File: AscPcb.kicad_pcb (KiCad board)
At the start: 2 copper layers, 116 x 78.7 mm, 83 parts, among them J1 12402012E212A, J10 Conn_01x02_Pin, J11 Conn_01x02_Pin, J12 Conn_01x02_Pin, J13 Conn_01x12_Pin, J14 Conn_01x02_Pin, J15 Conn_01x02_Pin, J16 Conn_01x02_Pin, J2 B2B-PH-K-S(LF)(SN), J3 Conn_01x02_Pin, J3 Conn_01x10_Pin, J4 Conn_01x06_Pin, J5 Screw_Terminal_01x02, J6 Conn_01x02_Pin, J7 Conn_01x02_Pin, J8 Conn_01x03_Pin, J9 Screw_Terminal_01x02, Q1 Q_NMOS_DGS, Q4 BC817, Q5 BC817, SW1 TL3305AF260QG, SW2 TL3305AF260QG, U1 ESP32-C3-WROOM-02-N4, U2 BQ24040DSQR, U3 TLV75801PDRVR, U4 CP2102N-A02-GQFN24R, U5 LTC3625EDE_PBF, U6 BMI270, U8 AP62300TWU

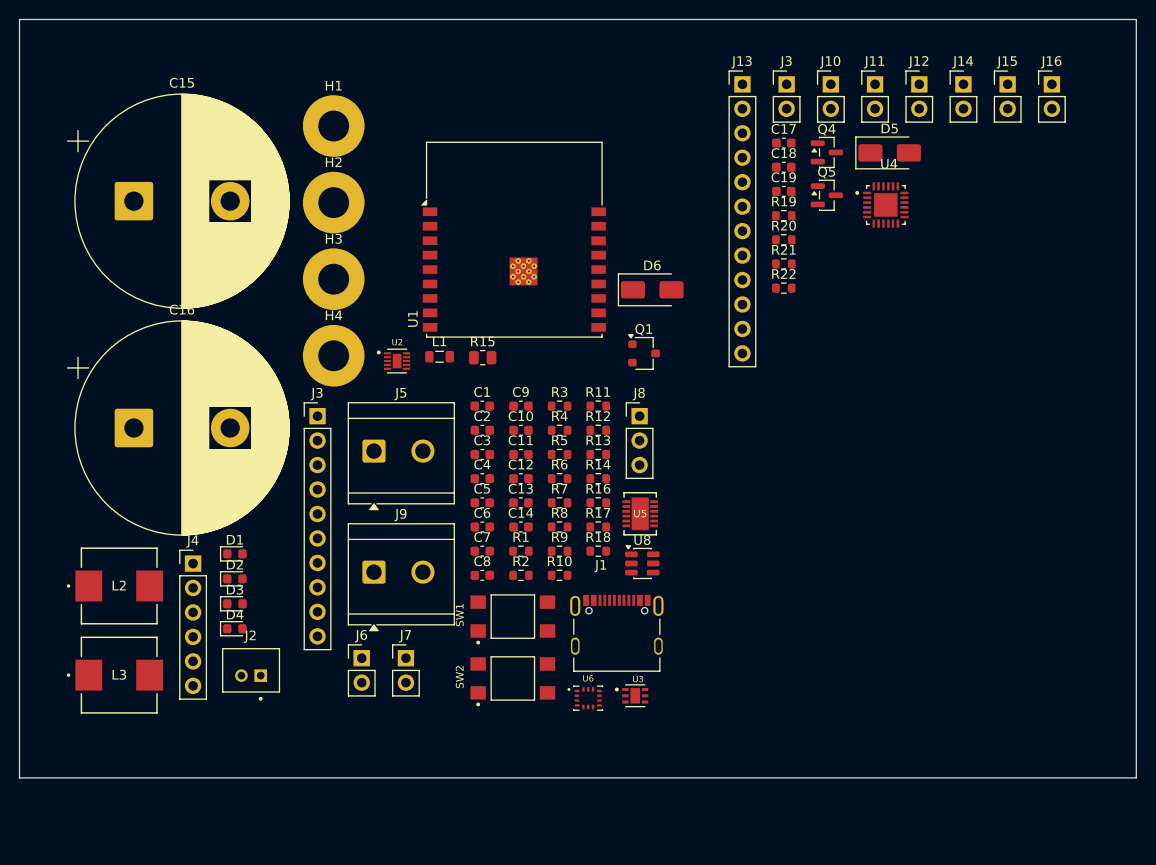
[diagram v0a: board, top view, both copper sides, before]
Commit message: add schmitt trigger
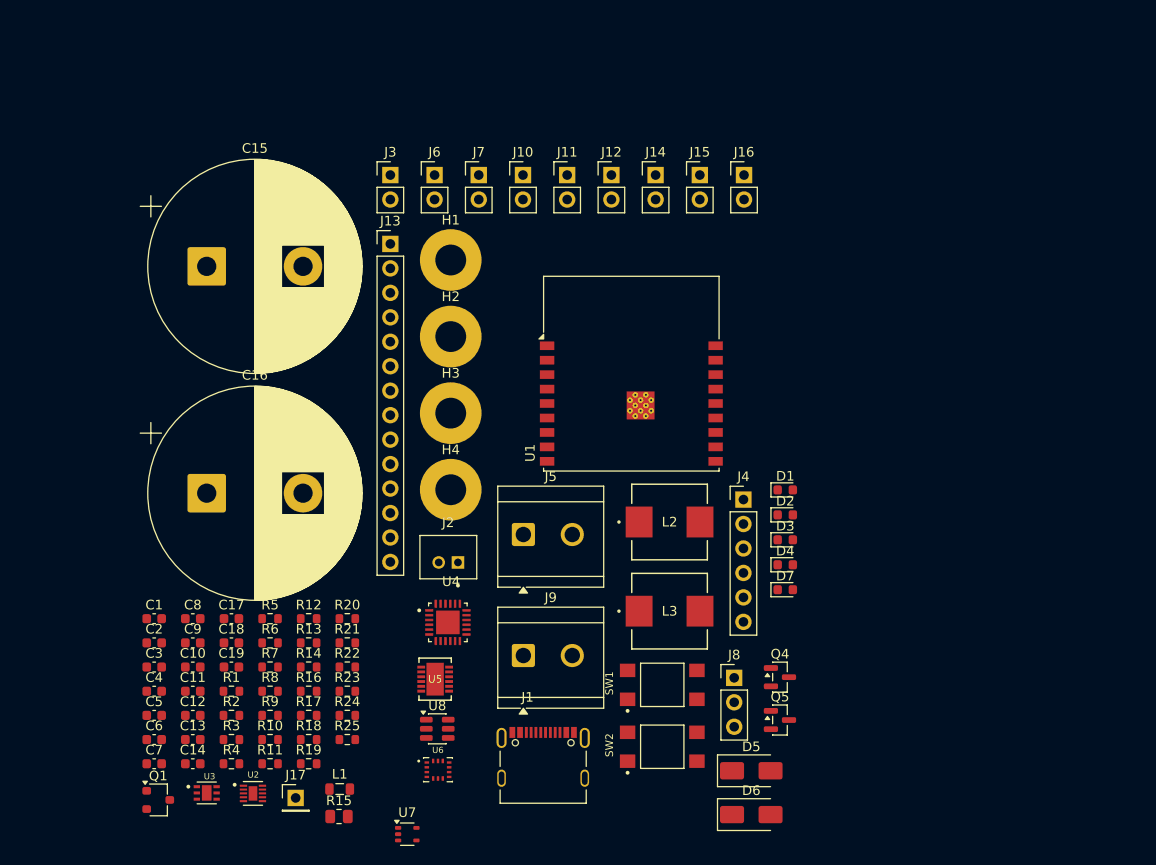
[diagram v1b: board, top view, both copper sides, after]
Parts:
- removed the J3 at (127.3, 84.1)
- removed the J3 at (176.0, 49.7)
- added D7: GREEN, LED_SMD:LED_0603_1608Metric, F.Cu at (175.9, 102.1)
- added J17: Conn_01x01_Pin, Connector_PinHeader_2.54mm:PinHeader_1x01_P2.54mm_Vertical, F.Cu at (125.1, 123.7)
- added J3: Conn_01x02_Pin, Connector_PinHeader_2.54mm:PinHeader_1x02_P2.54mm_Vertical, F.Cu at (134.9, 59.1)
- added R23: 10k, Resistor_SMD:R_0603_1608Metric, F.Cu at (130.4, 112.7)
- added R24: 10k, Resistor_SMD:R_0603_1608Metric, F.Cu at (130.4, 115.2)
- added R25: 150, Resistor_SMD:R_0603_1608Metric, F.Cu at (130.4, 117.7)
- added U7: 74LVC1G07, Package_TO_SOT_SMD:SOT-353_SC-70-5, F.Cu at (136.7, 127.5)
- J13: value Conn_01x12_Pin -> Conn_01x14_Pin; footprint Connector_PinHeader_2.54mm:PinHeader_1x12_P2.54mm_Vertical -> Connector_PinHeader_2.54mm:PinHeader_1x14_P2.54mm_Vertical
- moved C17 75.7 mm to (118.4, 105.1)
- moved C18 75.7 mm to (118.4, 107.6)
- moved C19 75.7 mm to (118.4, 110.2)
- moved R19 75.3 mm to (126.4, 120.2)
- moved Q1 68.5 mm to (110.8, 124.0)
- moved D5 65.7 mm to (172.4, 120.9)
- moved U4 62.8 mm to (140.9, 105.5)
- moved R22 60.0 mm to (130.4, 110.2)
- moved R20 60.0 mm to (130.4, 105.1)
- moved R21 60.0 mm to (130.4, 107.6)
- moved J4 57.5 mm to (171.6, 92.8)
- moved L2 57.5 mm to (163.9, 95.1)
- moved L3 57.5 mm to (163.9, 104.4)
- moved D1 57.5 mm to (175.9, 91.8)
- moved D2 57.5 mm to (175.9, 94.4)
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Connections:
- J13 pad 1: IO0 -> GND
- J13 pad 10: IO19 -> IO10
- J13 pad 11: ESP_TXD -> IO18
- J13 pad 12: ESP_RXD -> IO19
- J13 pad 2: IO1 -> +3V3
- J13 pad 3: IO3 -> IO0
- J13 pad 4: IO4 -> IO1
- J13 pad 5: IO5 -> IO3
- J13 pad 6: IO6 -> IO4
- J13 pad 7: IO7 -> IO5
- J13 pad 8: IO10 -> IO6
- J13 pad 9: IO18 -> IO7
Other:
- board outline removed

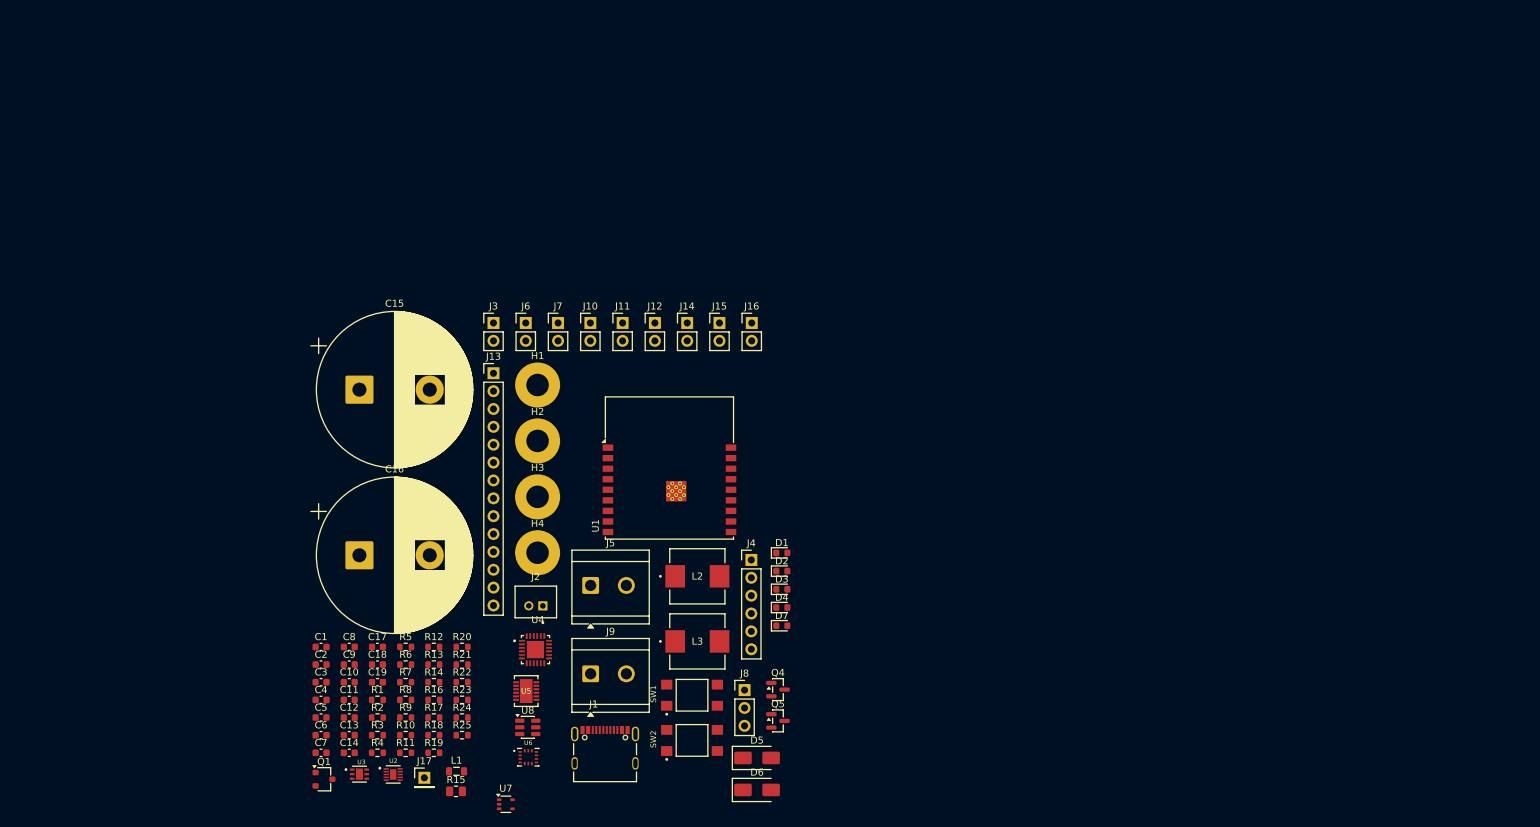
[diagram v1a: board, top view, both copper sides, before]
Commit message: started with pcb layout, did usb-c, buck, linear reg, bq24, cp2102
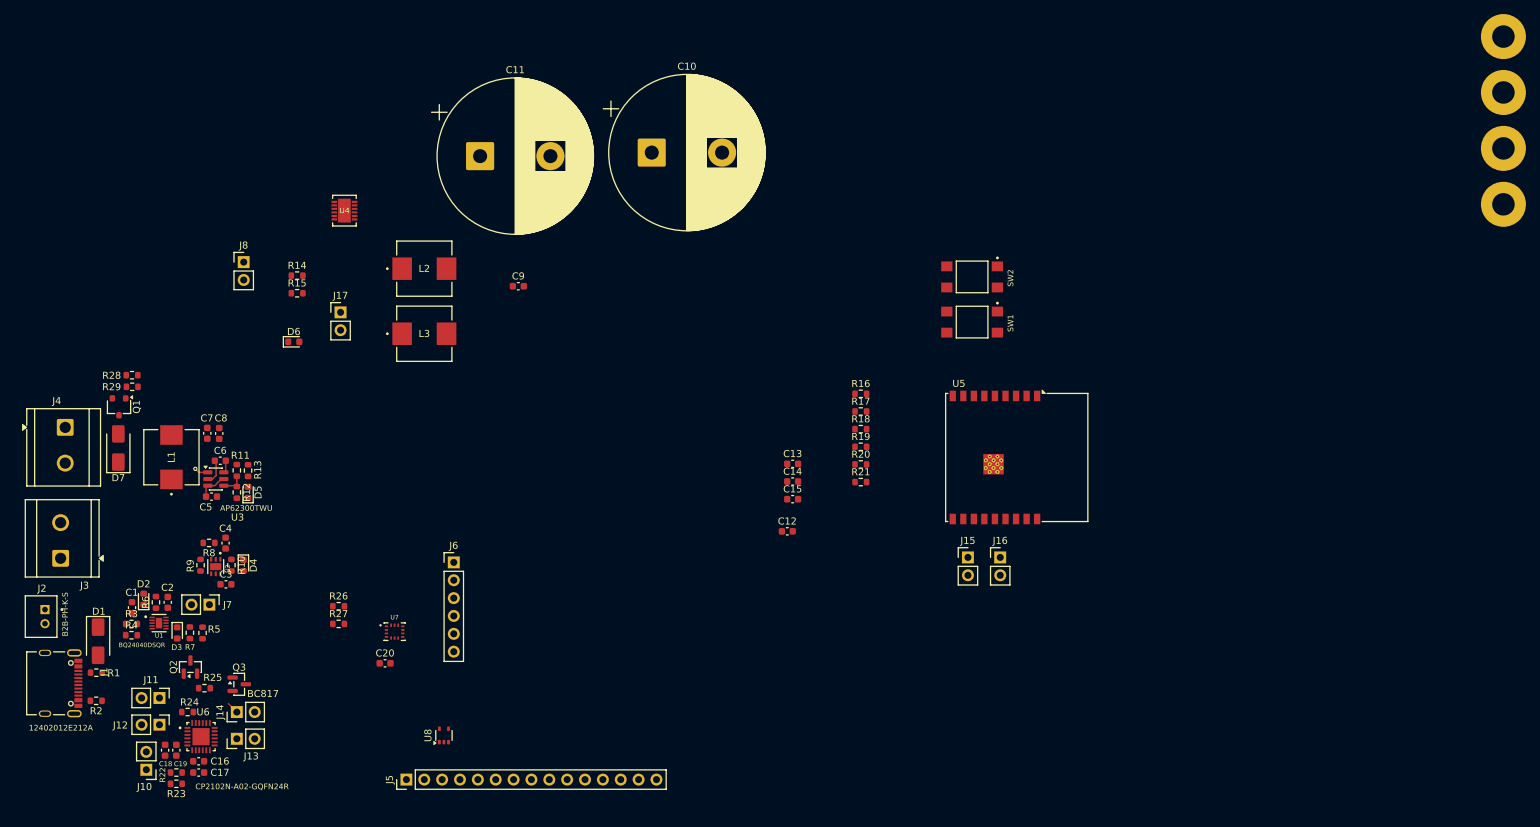
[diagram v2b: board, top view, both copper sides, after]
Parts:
- removed J9: Screw_Terminal_01x02, TerminalBlock_CUI:TerminalBlock_CUI_TB007-508-02_1x02_P5.08mm_Horizontal
- removed Q4, Q5: BC817, Package_TO_SOT_SMD:SOT-23
- added C20: 100nF, Capacitor_SMD:C_0603_1608Metric, F.Cu at (119.5, 107.5)
- added Q2: BC817, Package_TO_SOT_SMD:SOT-23, F.Cu at (91.8, 108.0)
- added Q3: BC817, Package_TO_SOT_SMD:SOT-23, F.Cu at (98.7, 110.5)
- added R26: 10k, Resistor_SMD:R_0603_1608Metric, F.Cu at (112.9, 99.4)
- added R27: 10k, Resistor_SMD:R_0603_1608Metric, F.Cu at (112.9, 101.9)
- added R28: 10k, Resistor_SMD:R_0603_1608Metric, F.Cu at (83.5, 66.5)
- added R29: 1k, Resistor_SMD:R_0603_1608Metric, F.Cu at (83.5, 68.2)
- C10: value 220nF -> 100F; footprint Capacitor_SMD:C_0603_1608Metric -> Capacitor_THT:CP_Radial_D22.0mm_P10.00mm_SnapIn
- C11: value 100nF -> 100F; footprint Capacitor_SMD:C_0603_1608Metric -> Capacitor_THT:CP_Radial_D22.0mm_P10.00mm_SnapIn
- C12: value 22uF -> 100nF
- C13: value 22uF -> 10uF
- C14: value 10uF -> 1uF
- C15: value 100F -> 1uF; footprint Capacitor_THT:CP_Radial_D22.0mm_P10.00mm_SnapIn -> Capacitor_SMD:C_0603_1608Metric
- C16: value 100F -> 100nF; footprint Capacitor_THT:CP_Radial_D22.0mm_P10.00mm_SnapIn -> Capacitor_SMD:C_0603_1608Metric
- C17: value 100nF -> 4.7uF
- C5: value 100nF -> 10uF
- C6: value 10uF -> 220nF
- C7, C8: value 1uF -> 22uF
- D1, D7: value GREEN -> D_Schottky; footprint LED_SMD:LED_0603_1608Metric -> Diode_SMD:D_SMA
- D2: value RED -> GREEN
- D3: value GREEN -> RED
- D5, D6: value D_Schottky -> GREEN; footprint Diode_SMD:D_SMA -> LED_SMD:LED_0603_1608Metric
- J13: value Conn_01x14_Pin -> Conn_01x02_Pin; footprint Connector_PinHeader_2.54mm:PinHeader_1x14_P2.54mm_Vertical -> Connector_PinHeader_2.54mm:PinHeader_1x02_P2.54mm_Vertical
- J17: value Conn_01x01_Pin -> Conn_01x02_Pin; footprint Connector_PinHeader_2.54mm:PinHeader_1x01_P2.54mm_Vertical -> Connector_PinHeader_2.54mm:PinHeader_1x02_P2.54mm_Vertical
- J2: value B2B-PH-K-S(LF)(SN) -> B2B-PH-K-S
- J3: value Conn_01x02_Pin -> Screw_Terminal_01x02; footprint Connector_PinHeader_2.54mm:PinHeader_1x02_P2.54mm_Vertical -> TerminalBlock_CUI:TerminalBlock_CUI_TB007-508-02_1x02_P5.08mm_Horizontal
- J4: value Conn_01x06_Pin -> Screw_Terminal_01x02; footprint Connector_PinHeader_2.54mm:PinHeader_1x06_P2.54mm_Vertical -> TerminalBlock_CUI:TerminalBlock_CUI_TB007-508-02_1x02_P5.08mm_Horizontal
- J5: value Screw_Terminal_01x02 -> Conn_01x15_Pin; footprint TerminalBlock_CUI:TerminalBlock_CUI_TB007-508-02_1x02_P5.08mm_Horizontal -> Connector_PinHeader_2.54mm:PinHeader_1x15_P2.54mm_Vertical
- J6: value Conn_01x02_Pin -> Conn_01x06_Pin; footprint Connector_PinHeader_2.54mm:PinHeader_1x02_P2.54mm_Vertical -> Connector_PinHeader_2.54mm:PinHeader_1x06_P2.54mm_Vertical
- J8: value Conn_01x03_Pin -> Conn_01x02_Pin; footprint Connector_PinHeader_2.54mm:PinHeader_1x03_P2.54mm_Vertical -> Connector_PinHeader_2.54mm:PinHeader_1x02_P2.54mm_Vertical
- L1: footprint Inductor_SMD:L_0805_2012Metric -> DR73-3R3-R:DR73-3R3-R_EAT
- R10, R13: value 10k -> 150
- R11: value 10k -> 33.2k
- R14: value 10k -> 61.9k
- R15: value 33.2k -> 150; footprint Resistor_SMD:R_0805_2012Metric -> Resistor_SMD:R_0603_1608Metric
- R17, R25, R5: value 150 -> 10k
- R18: value 61.9k -> 10k
- R21: value 1k -> 10k
- R22: value 10k -> 22.1k
- R23: value 10k -> 47.5k
- R3: value 536 -> 1k
- R4: value 150 -> 2k
- R6: value 49.9k -> 1.5k
- R7: value 10k -> 1.5k
- R8: value 150 -> 49.9k
- U1: value ESP32-C3-WROOM-02-N4 -> BQ24040DSQR; footprint RF_Module:ESP32-C3-WROOM-02 -> BQ24040DSQR:SON40P200X200X80-11N
- U2: value BQ24040DSQR -> TLV75801PDRVR; footprint BQ24040DSQR:SON40P200X200X80-11N -> TLV75801PDRVR:SON65P200X200X80-7N
- U3: value TLV75801PDRVR -> AP62300TWU; footprint TLV75801PDRVR:SON65P200X200X80-7N -> Package_TO_SOT_SMD:TSOT-23-6
- U4: value CP2102N-A02-GQFN24R -> LTC3625EDE_PBF; footprint CP2102N-A02-GQFN24R:QFN50P400X400X80-25N -> LTC3625EDE_PBF:DFN-12_DE
- U5: value LTC3625EDE_PBF -> ESP32-C3-WROOM-02-N4; footprint LTC3625EDE_PBF:DFN-12_DE -> RF_Module:ESP32-C3-WROOM-02
- U6: value BMI270 -> CP2102N-A02-GQFN24R; footprint BMI270:XDCR_BMI270 -> CP2102N-A02-GQFN24R:QFN50P400X400X80-25N
- U7: value 74LVC1G07 -> BMI270; footprint Package_TO_SOT_SMD:SOT-353_SC-70-5 -> BMI270:XDCR_BMI270
- U8: value AP62300TWU -> 74LVC1G07; footprint Package_TO_SOT_SMD:TSOT-23-6 -> Package_TO_SOT_SMD:SOT-353_SC-70-5
- moved H1 146.0 mm to (278.5, 18.4)
- moved H2 146.0 mm to (278.5, 26.3)
- moved H3 146.0 mm to (278.5, 34.2)
- moved H4 146.0 mm to (278.5, 42.2)
- moved J4 99.4 mm to (74.0, 73.9), turned to -90 degrees
- moved D1 98.0 mm to (78.7, 104.3), turned to -90 degrees
- moved D7 97.7 mm to (81.5, 76.8), turned to 90 degrees
- moved J8 93.7 mm to (99.4, 50.4)
- moved D6 91.7 mm to (106.5, 61.8)
- moved D2 90.8 mm to (85.2, 98.3), turned to 90 degrees
- moved J12 90.7 mm to (87.4, 116.2), turned to -90 degrees
- moved J10 89.6 mm to (85.5, 122.6), turned to 180 degrees
- moved C10 86.7 mm to (157.4, 34.9)
- moved D3 86.2 mm to (89.9, 103.2), turned to -90 degrees
- moved J11 84.7 mm to (87.4, 112.4), turned to -90 degrees
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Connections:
- C1 pad 1: +5V -> GND
- C1 pad 2: GND -> +5V
- C10 pad 1: Net-(U8-SW) -> Net-(U4-VMID)
- C10 pad 2: Net-(U8-BST) -> Net-(J8-Pin_2)
- C11 pad 1: +3V3 -> GND
- C11 pad 2: GND -> Net-(U4-VMID)
- C12 pad 1: 3V3LTC -> +3V3
- C13 pad 1: 3V3LTC -> +3V3
- C14 pad 1: GND -> EN
- C14 pad 2: 3V3LTC -> GND
- C15 pad 1: Net-(U5-VMID) -> IO9
- C15 pad 2: Net-(J7-Pin_2) -> GND
- C16 pad 2: Net-(U5-VMID) -> Net-(U6-VBUS)
- C17 pad 2: Net-(U4-VDD) -> Net-(U6-VBUS)
- C18 pad 2: Net-(J10-Pin_1) -> Net-(U6-VDD)
- C19 pad 1: GND -> Net-(U6-VDD)
- C19 pad 2: Net-(J10-Pin_1) -> GND
- C2 pad 1: Net-(J6-Pin_2) -> Net-(J7-Pin_2)
- C5 pad 1: +3V3 -> GND
- C5 pad 2: GND -> +12V
- C6 pad 1: +3V3 -> Net-(U3-SW)
- C6 pad 2: GND -> Net-(U3-BST)
- C7 pad 1: EN -> 3V3LTC
- C8 pad 1: IO9 -> 3V3LTC
- C9 pad 2: +12V -> Net-(J17-Pin_1)
- D1 pad 1: Net-(D1-K) -> +5V
- D3 pad 1: GND -> Net-(D3-K)
- D5 pad 1: +5V -> GND
- D6 pad 1: +12V -> GND
- D7 pad 1: GND -> +12V
- J1 pad A4_B9: Net-(D5-A) -> Net-(D1-A)
- J1 pad B4_A9: Net-(D5-A) -> Net-(D1-A)
- J13 pad 1: GND -> Net-(J13-Pin_1)
- J13 pad 2: +3V3 -> ESP_TXD
- J14 pad 1: IO19 -> Net-(J14-Pin_1)
- J14 pad 2: D+ -> ESP_RXD
- J15 pad 1: Net-(J15-Pin_1) -> IO18
- J15 pad 2: ESP_TXD -> D-
- J16 pad 1: Net-(J16-Pin_1) -> IO19
- J16 pad 2: ESP_RXD -> D+
- J2 pad 1: Net-(J6-Pin_2) -> Net-(J7-Pin_2)
- J3 pad 1: IO18 -> GND
- J3 pad 2: D- -> +12V
- J4 pad 1: OSDO -> Net-(D7-A)
- J4 pad 2: OSCB -> +12V
- J5 pad 2: +12V -> +3V3
- J6 pad 1: POWER -> OSDO
- J6 pad 2: Net-(J6-Pin_2) -> OSCB
- J8 pad 1: Net-(J8-Pin_1) -> POWER
- L1 pad 1: Net-(U8-SW) -> Net-(U3-SW)
- L2 pad 1: Net-(U5-SW1) -> Net-(U4-SW1)
- L2 pad 2: Net-(U5-VMID) -> Net-(U4-VMID)
- L3 pad 1: Net-(U5-SW2) -> Net-(U4-SW2)
- L3 pad 2: Net-(U5-VMID) -> Net-(U4-VMID)
- Q1 pad 1: Net-(D6-A) -> Net-(D7-A)
- R10 pad 2: IO9 -> Net-(D4-A)
- R11 pad 1: +3V3 -> 3V3LTC
- R11 pad 2: Net-(U1-IO8) -> Net-(U3-FB)
- R12 pad 1: Net-(U1-IO2) -> Net-(U3-FB)
- R12 pad 2: +3V3 -> GND
- R13 pad 1: +3V3 -> 3V3LTC
- R13 pad 2: IO1 -> Net-(D5-A)
- R14 pad 1: +3V3 -> Net-(U4-PROG)
- R14 pad 2: IO0 -> GND
- R15 pad 1: 3V3LTC -> Net-(J8-Pin_2)
- R15 pad 2: Net-(U8-FB) -> Net-(D6-A)
- R16 pad 1: Net-(U8-FB) -> +3V3
- R16 pad 2: GND -> EN
- R17 pad 1: 3V3LTC -> Net-(U5-IO2)
- R17 pad 2: Net-(D4-A) -> +3V3
- R18 pad 1: Net-(U5-PROG) -> +3V3
- R18 pad 2: GND -> Net-(U5-IO8)
- R19 pad 1: DTR -> +3V3
- R19 pad 2: Net-(Q5-B) -> IO9
- R20 pad 1: RTS -> IO5
- R20 pad 2: Net-(Q4-B) -> POWER
- R21 pad 1: Net-(Q1-G) -> IO5
- R21 pad 2: IO3 -> GND
- R22 pad 1: IO3 -> Net-(U6-VBUS)
- R22 pad 2: GND -> Net-(J10-Pin_1)
- R23 pad 1: IO5 -> Net-(U6-VBUS)
- R23 pad 2: POWER -> GND
- R24 pad 1: IO5 -> DTR
- R24 pad 2: GND -> Net-(Q2-B)
- R25 pad 1: Net-(J7-Pin_2) -> RTS
- R25 pad 2: Net-(D7-A) -> Net-(Q3-B)
- R3 pad 1: Net-(U2-ISET) -> GND
- R3 pad 2: GND -> Net-(U1-ISET)
- R4 pad 1: Net-(J6-Pin_2) -> GND
- R4 pad 2: Net-(D1-A) -> Net-(U1-PRETERM)
- R5 pad 1: Net-(J6-Pin_2) -> GND
- R5 pad 2: Net-(D2-A) -> Net-(U1-TS)
- R6 pad 1: +3V3 -> Net-(J7-Pin_2)
- R6 pad 2: Net-(U3-FB) -> Net-(D2-A)
- R7 pad 1: Net-(U3-FB) -> Net-(J7-Pin_2)
- R7 pad 2: GND -> Net-(D3-A)
- R8 pad 2: Net-(D3-A) -> Net-(U2-FB)
- R9 pad 1: +3V3 -> Net-(U2-FB)
- R9 pad 2: EN -> GND
- U1 pad 1: +3V3 -> +5V
- U1 pad 10: IO10 -> Net-(J7-Pin_2)
- U1 pad 11: ESP_RXD -> GND
- U1 pad 2: EN -> Net-(U1-ISET)
- U1 pad 3: IO4 -> GND
- U1 pad 4: IO5 -> Net-(U1-PRETERM)
- U1 pad 5: IO6 -> Net-(D2-K)
- U1 pad 6: IO7 -> (no net)
- U1 pad 7: Net-(U1-IO8) -> +5V
- U1 pad 8: IO9 -> Net-(D3-K)
- U1 pad 9: GND -> Net-(U1-TS)
- U2 pad 1: +5V -> +3V3
- U2 pad 2: Net-(U2-ISET) -> Net-(U2-FB)
- U2 pad 4: unconnected-(U2-PRETERM-Pad4) -> POWER
- U2 pad 5: Net-(D1-K) -> unconnected-(U2-DNC-Pad5)
- U2 pad 6: (no net) -> POWER
- U2 pad 7: +5V -> (no net)
- U3 pad 1: +3V3 -> GND
- U3 pad 2: Net-(U3-FB) -> Net-(U3-SW)
- U3 pad 3: GND -> +12V
- U3 pad 4: POWER -> Net-(U3-FB)
- U3 pad 5: unconnected-(U3-DNC-Pad5) -> +12V
- U3 pad 6: POWER -> Net-(U3-BST)
- U4 pad 1: unconnected-(U4-~{RI}/CLK-Pad1) -> Net-(U4-SW1)
- U4 pad 10: (no net) -> Net-(U4-VMID)
- U4 pad 11: unconnected-(U4-GPIO.3/WAKEUP-Pad11) -> Net-(J8-Pin_2)
- U4 pad 12: unconnected-(U4-GPIO.2/RS485-Pad12) -> Net-(U4-SW2)
- U4 pad 13: unconnected-(U4-GPIO.1/RXT-Pad13) -> GND
- U4 pad 2: GND -> Net-(J17-Pin_1)
- U4 pad 3: Net-(J11-Pin_1) -> GND
- U4 pad 4: Net-(J12-Pin_1) -> GND
- U4 pad 5: unconnected-(U4-VIO-Pad5) -> Net-(J17-Pin_1)
- U4 pad 6: Net-(U4-VDD) -> Net-(U4-PROG)
- U4 pad 7: Net-(J10-Pin_1) -> Net-(J17-Pin_1)
- U4 pad 8: Net-(J10-Pin_1) -> unconnected-(U4-*PFO-Pad8)
- U5 pad 1: Net-(U5-SW1) -> +3V3
- U5 pad 10: Net-(U5-VMID) -> IO10
- U5 pad 11: Net-(J7-Pin_2) -> ESP_RXD
- U5 pad 12: Net-(U5-SW2) -> ESP_TXD
- U5 pad 13: GND -> IO18
- U5 pad 2: 3V3LTC -> EN
- U5 pad 3: GND -> IO4
- U5 pad 4: GND -> IO5
- U5 pad 5: 3V3LTC -> IO6
- U5 pad 6: Net-(U5-PROG) -> IO7
- U5 pad 7: Net-(J8-Pin_1) -> Net-(U5-IO8)
- U5 pad 8: Net-(J8-Pin_2) -> IO9
- U5 pad 9: Net-(J8-Pin_3) -> GND
- U6 pad 1: GND -> unconnected-(U6-~{RI}/CLK-Pad1)
- U6 pad 10: OSCB -> (no net)
- U6 pad 11: OSDO -> unconnected-(U6-GPIO.3/WAKEUP-Pad11)
- U6 pad 12: +3V3 -> unconnected-(U6-GPIO.2/RS485-Pad12)
- U6 pad 13: IO1 -> unconnected-(U6-GPIO.1/RXT-Pad13)
- U6 pad 14: IO0 -> unconnected-(U6-GPIO.0/TXT-Pad14)
- U6 pad 2: ASDX -> GND
- U6 pad 3: ASCX -> Net-(J11-Pin_1)
- U6 pad 4: INT1 -> Net-(J12-Pin_1)
- U6 pad 5: +3V3 -> Net-(U6-VDD)
- U6 pad 6: GND -> Net-(U6-VDD)
- U6 pad 7: GND -> Net-(U6-VBUS)
- U6 pad 8: +3V3 -> Net-(U6-VBUS)
- U6 pad 9: INT2 -> unconnected-(U6-~{RST}-Pad9)
- U7 pad 1: unconnected-(U7-NC-Pad1) -> GND
- U7 pad 2: Net-(J17-Pin_1) -> ASDX
- U7 pad 3: GND -> ASCX
- U7 pad 4: IO6 -> INT1
- U8 pad 1: GND -> unconnected-(U8-NC-Pad1)
- U8 pad 2: Net-(U8-SW) -> LIGHT
- U8 pad 3: +12V -> GND
- U8 pad 4: Net-(U8-FB) -> IO6
- U8 pad 5: +12V -> +3V3
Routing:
- net +12V: track 0.00 -> 4.32 mm
- net Net-(U3-SW): track 0.00 -> 3.55 mm
- net Net-(U3-FB): track 0.00 -> 3.42 mm
- net GND: track 0.00 -> 1.98 mm, vias 0 -> 1
- net Net-(U3-BST): track 0.00 -> 1.76 mm
- net Net-(J14-Pin_1): track 0.00 -> 1.70 mm

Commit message: board layout done but not wired
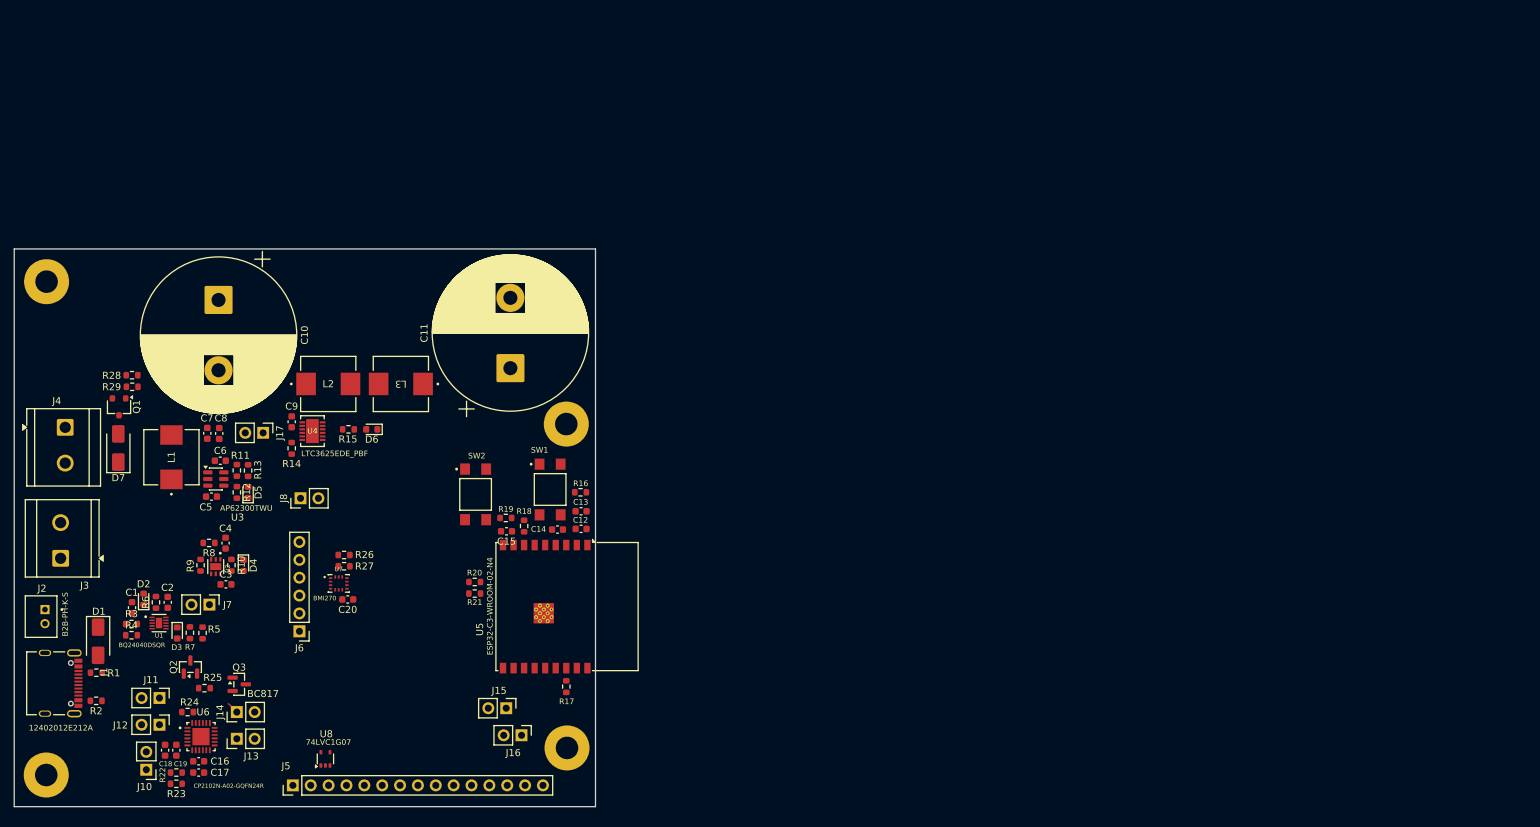
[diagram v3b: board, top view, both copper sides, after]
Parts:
- moved H1 232.3 mm to (71.3, 123.3)
- moved H2 208.9 mm to (71.3, 53.2)
- moved H4 154.0 mm to (145.3, 119.5)
- moved H3 138.9 mm to (145.2, 73.5)
- moved SW2 77.1 mm to (132.3, 83.5), turned to -90 degrees
- moved J16 72.6 mm to (138.9, 117.7), turned to -90 degrees
- moved J15 69.1 mm to (136.7, 113.8), turned to -90 degrees
- moved U5 67.4 mm to (142.2, 99.4)
- moved C10 65.1 mm to (95.8, 55.8), turned to -90 degrees
- moved SW1 64.5 mm to (142.9, 82.8), turned to -90 degrees
- moved R20 57.4 mm to (132.2, 95.9), turned to 180 degrees
- moved R17 57.3 mm to (145.2, 110.8), turned to 90 degrees
- moved R21 57.1 mm to (132.2, 97.5), turned to 180 degrees
- moved R19 51.5 mm to (136.7, 86.8), turned to 180 degrees
- moved R18 49.8 mm to (139.2, 88.0), turned to -90 degrees
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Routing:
- net +12V: track 4.32 -> 0.00 mm
- net Net-(U3-SW): track 3.55 -> 0.00 mm
- net Net-(U3-FB): track 3.42 -> 0.00 mm
- net GND: track 1.98 -> 0.00 mm, vias 1 -> 0
- net Net-(U3-BST): track 1.76 -> 0.00 mm
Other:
- board outline added: 82.7 x 79.3 mm

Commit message: first attempt at putting down traces
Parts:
- removed J11, J12, J13, J14: Conn_01x02_Pin, Connector_PinHeader_2.54mm:PinHeader_1x02_P2.54mm_Vertical
- J2: value B2B-PH-K-S -> B2B-PH-K-S(LF)(SN)
- moved R1 6.35 mm to (84.7, 107.8)
- moved R2 4.48 mm to (80.8, 116.5), turned to -90 degrees
- moved J15 1.53 mm to (135.2, 113.9)
- turned R17 to -90 degrees
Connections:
- U6 pad 20: Net-(J13-Pin_1) -> ESP_TXD
- U6 pad 21: Net-(J14-Pin_1) -> ESP_RXD
- U6 pad 3: Net-(J11-Pin_1) -> D+
- U6 pad 4: Net-(J12-Pin_1) -> D-
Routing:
- net D+: track 0.00 -> 77.8 mm, vias 0 -> 5
- net D-: track 0.00 -> 76.4 mm, vias 0 -> 4
- net Net-(U4-VMID): track 0.00 -> 60.8 mm, vias 0 -> 2
- net ESP_TXD: track 0.00 -> 50.1 mm
- net ESP_RXD: track 0.00 -> 49.2 mm
- net POWER: track 0.00 -> 38.0 mm
- net Net-(J7-Pin_2): track 0.00 -> 35.4 mm
- net +12V: track 0.00 -> 35.2 mm
- net +5V: track 0.00 -> 34.2 mm, vias 0 -> 4
- net Net-(J8-Pin_2): track 0.00 -> 33.6 mm, vias 0 -> 2
- net GND: track 0.00 -> 22.6 mm, vias 0 -> 14
- net 3V3LTC: track 0.00 -> 17.5 mm
- net OSDO: track 0.00 -> 17.0 mm
- net Net-(U4-SW2): track 0.00 -> 16.8 mm
- net Net-(J17-Pin_1): track 0.00 -> 16.6 mm
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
